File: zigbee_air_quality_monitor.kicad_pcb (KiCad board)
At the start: 4 copper layers, 19.8 x 50.9 mm, 37 parts, among them J1 USB_C_Receptacle_USB2.0, J2 QWIIC, J3 Conn_02x02_Odd_Even, SW1 PAIR_BTN, SW2 USER_BTN, U1 USBLC6-2SC6, U2 BT840, U3 XC6206P332MR, U4 SCD41-D-R2, U6 TXS0102DCU

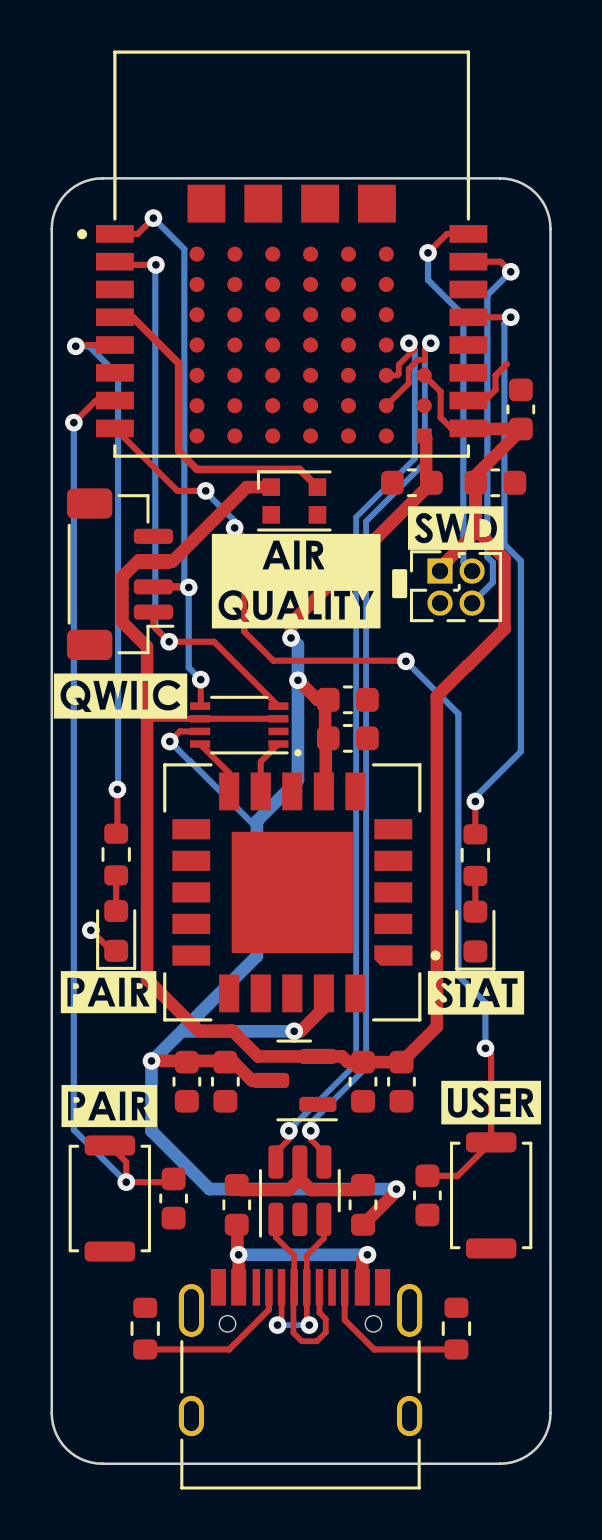
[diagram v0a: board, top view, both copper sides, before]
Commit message: Added inner GND planes, backside silkscreen label
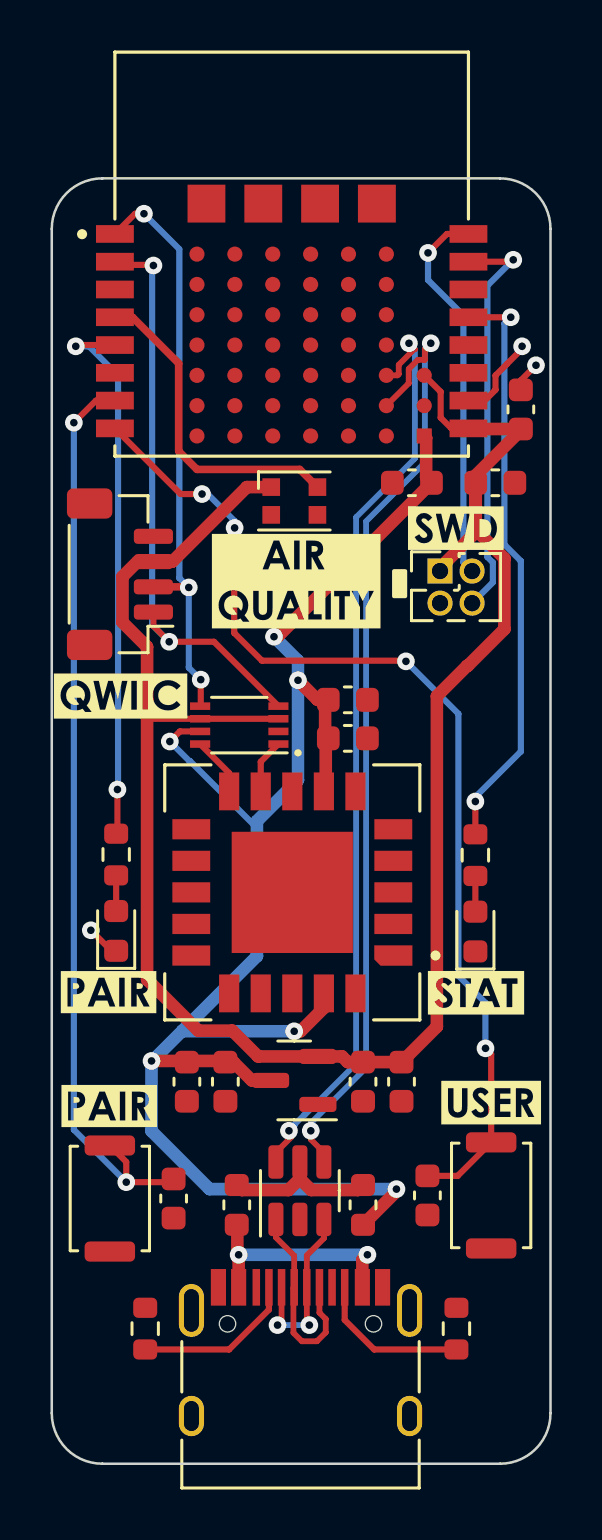
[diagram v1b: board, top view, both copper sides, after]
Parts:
- added G***: LOGO, LOGO, B.Cu at (131.7, 95.8)
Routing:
- net GND: track 3.80 -> 5.97 mm, vias 1 -> 3
- net VCC: track 68.5 -> 69.1 mm
- added copper zone on In1.Cu, net GND
- added copper zone on In2.Cu, net GND
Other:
- board text added: "Jan Gnip rev1 03/24"

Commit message: Routing done, via stitching done
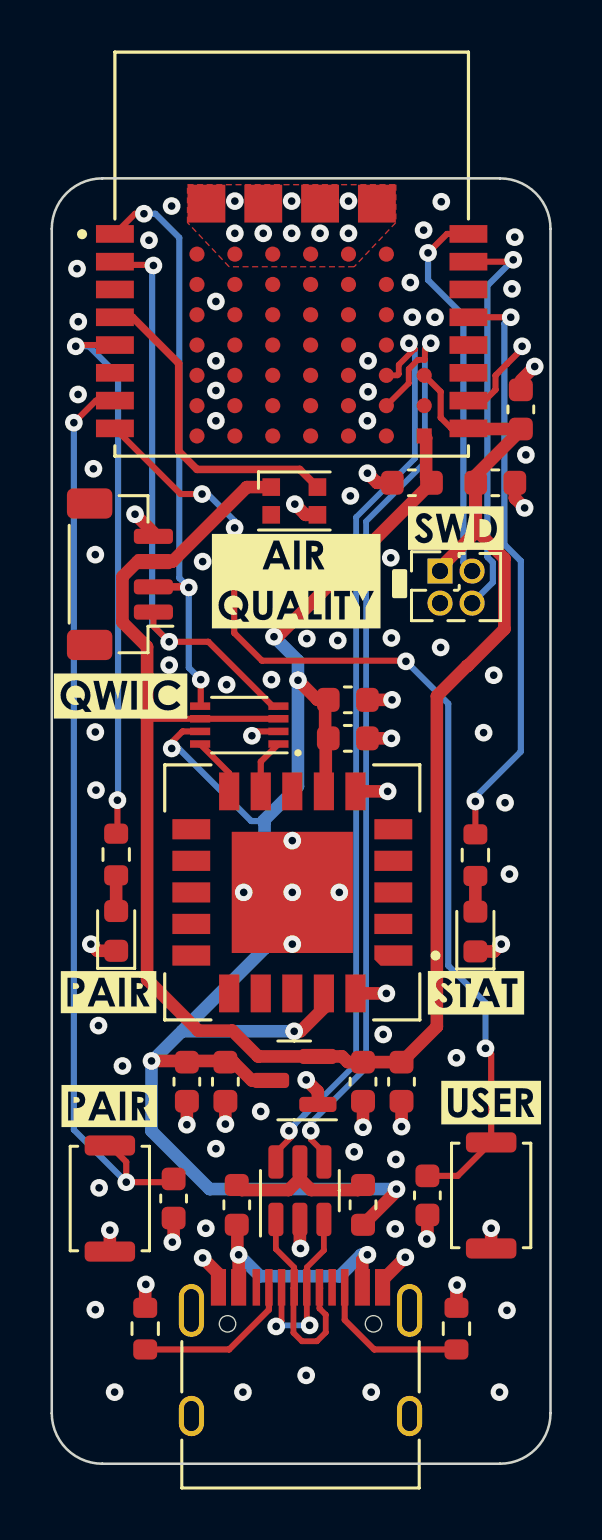
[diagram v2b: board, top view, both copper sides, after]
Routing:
- net GND: track 5.97 -> 31.5 mm, vias 3 -> 96
- net /USB_FUSE: track 8.98 -> 9.69 mm
- added copper zone on F.Cu, net GND

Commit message: Fixed silkscreen logo designator to make KiBot happy
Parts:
- renumbered G*** to G1
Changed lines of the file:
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@@
     (at 131.7 95.85 180)
     (attr board_only exclude_from_pos_files exclude_from_bom)
-    (fp_text reference "G***" (at 0 0) (layer "B.SilkS") hide
+    (fp_text reference "G1" (at 0 0) (layer "B.SilkS") hide
         (effects (font (size 1.524 1.524) (thickness 0.3)) (justify mirror))
     )

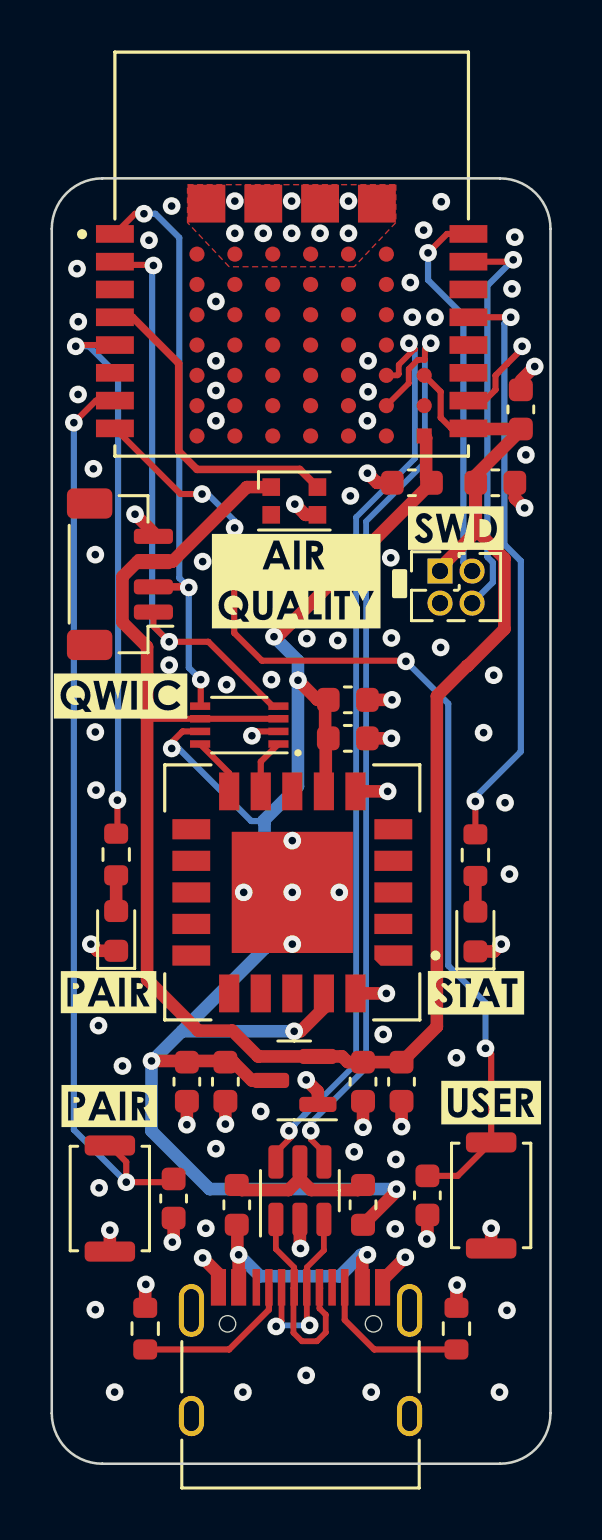
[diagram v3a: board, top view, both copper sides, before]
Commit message: Fixed QWIIC connector footprint and model
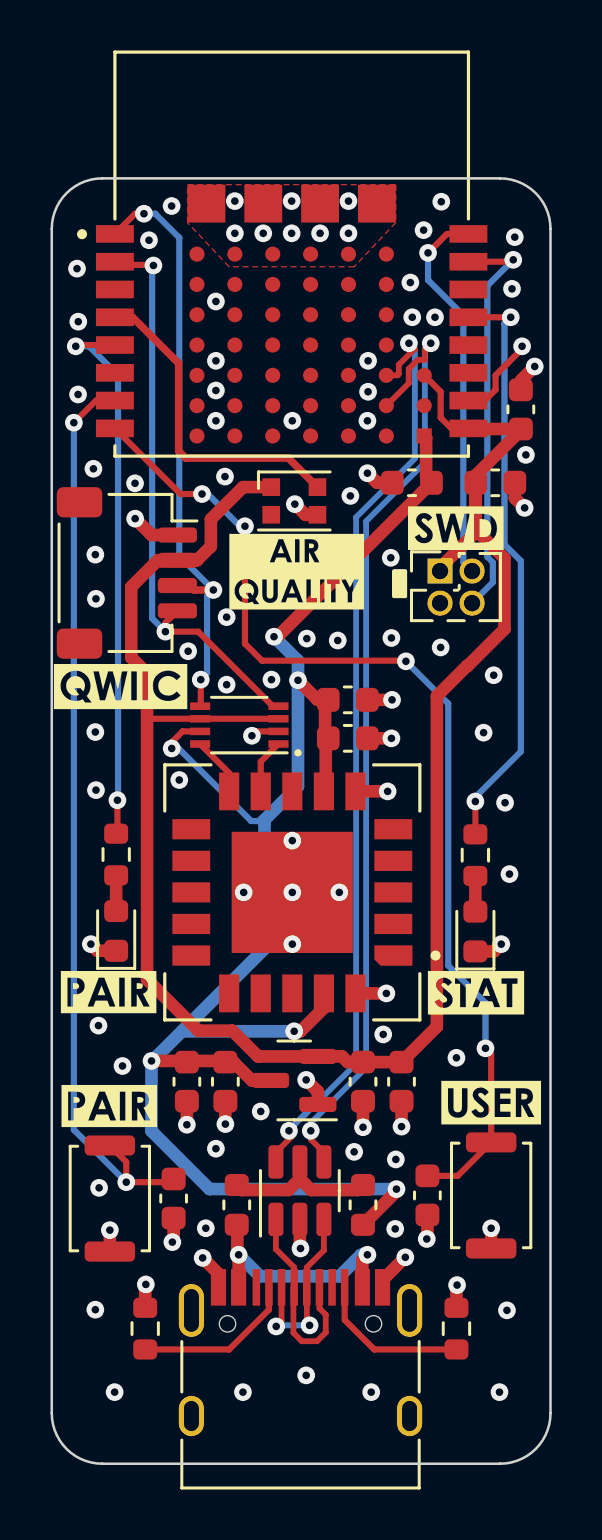
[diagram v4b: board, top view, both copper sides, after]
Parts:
- J2: footprint Connector_JST:JST_SH_BM04B-SRSS-TB_1x04-1MP_P1.00mm_Vertical -> Connector_JST:JST_SH_SM04B-SRSS-TB_1x04-1MP_P1.00mm_Horizontal
- kibuzzard-63D64589: footprint kibuzzard-63D64589 -> footprint
- moved kibuzzard-63D64589 0.38 mm to (131.8, 104.8)
- moved kibuzzard-63D6450F 0.38 mm to (124.8, 109.3)
- moved J2 0.28 mm to (125.1, 104.8), turned to -90 degrees
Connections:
- J1 pad S1: unconnected-(J1-SHIELD-PadS1) -> (no net)
- J2 pad 1: /I2C_SCL_3V3 -> GND
- J2 pad 2: /I2C_SDA_3V3 -> +3.3V
- J2 pad 3: +3.3V -> /I2C_SDA_3V3
- J2 pad 4: GND -> /I2C_SCL_3V3
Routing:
- net GND: track 31.5 -> 32.3 mm, vias 96 -> 101
- net /I2C_SCL_3V3: track 23.6 -> 23.0 mm

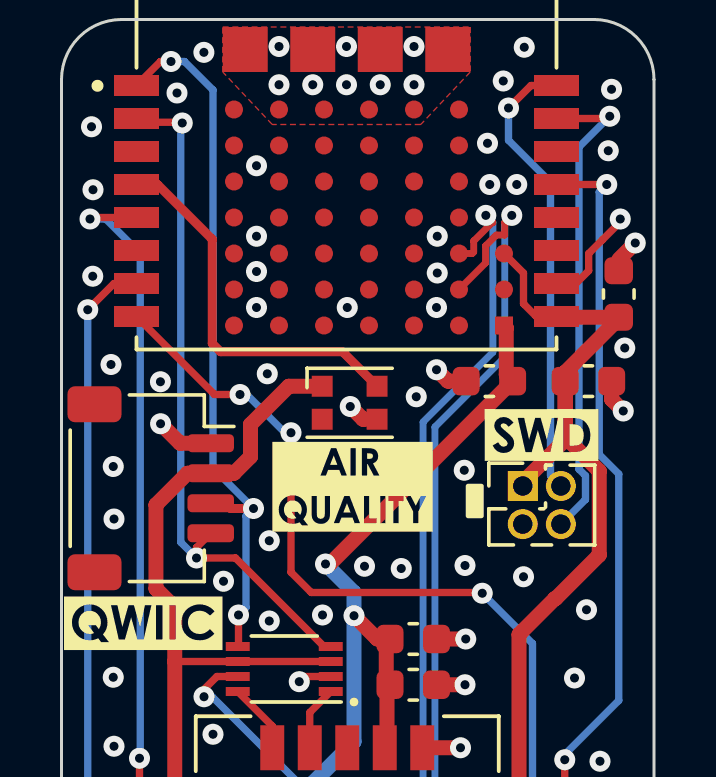
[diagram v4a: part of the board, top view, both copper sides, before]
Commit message: Changed supply voltage for WS2812-2020 LED to 5V
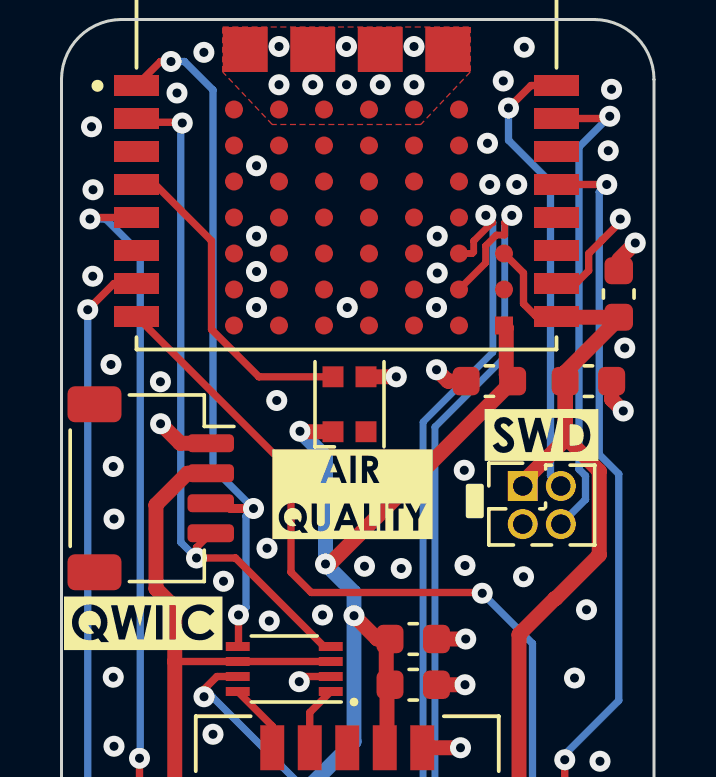
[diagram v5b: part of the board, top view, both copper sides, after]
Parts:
- moved kibuzzard-63D64589 0.25 mm to (131.8, 105.0)
- moved D3 0.05 mm to (131.7, 102.0), turned to 90 degrees
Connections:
- D3 pad 1: +3.3V -> VCC
- J1 pad S1: (no net) -> unconnected-(J1-SHIELD-PadS1)
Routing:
- net VCC: track 69.1 -> 75.0 mm, vias 6 -> 7
- net +3.3V: track 77.6 -> 72.1 mm
- net /AIR_QUALITY_LED: track 12.8 -> 10.9 mm
- net /USER_BTN: track 41.6 -> 40.8 mm, vias 4 -> 2
- net GND: track 32.3 -> 32.2 mm, vias 101 -> 100

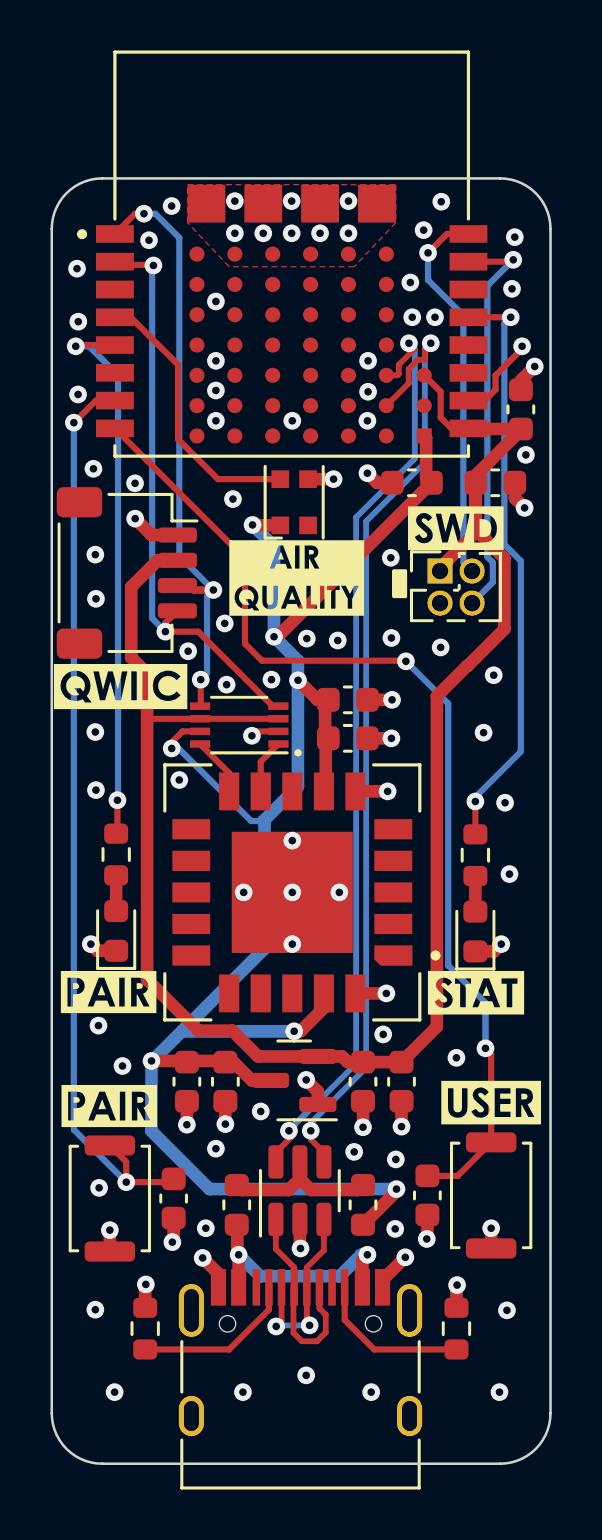
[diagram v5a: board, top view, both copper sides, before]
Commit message: Fixed clipped silkscreen, ERC+DRC warnings
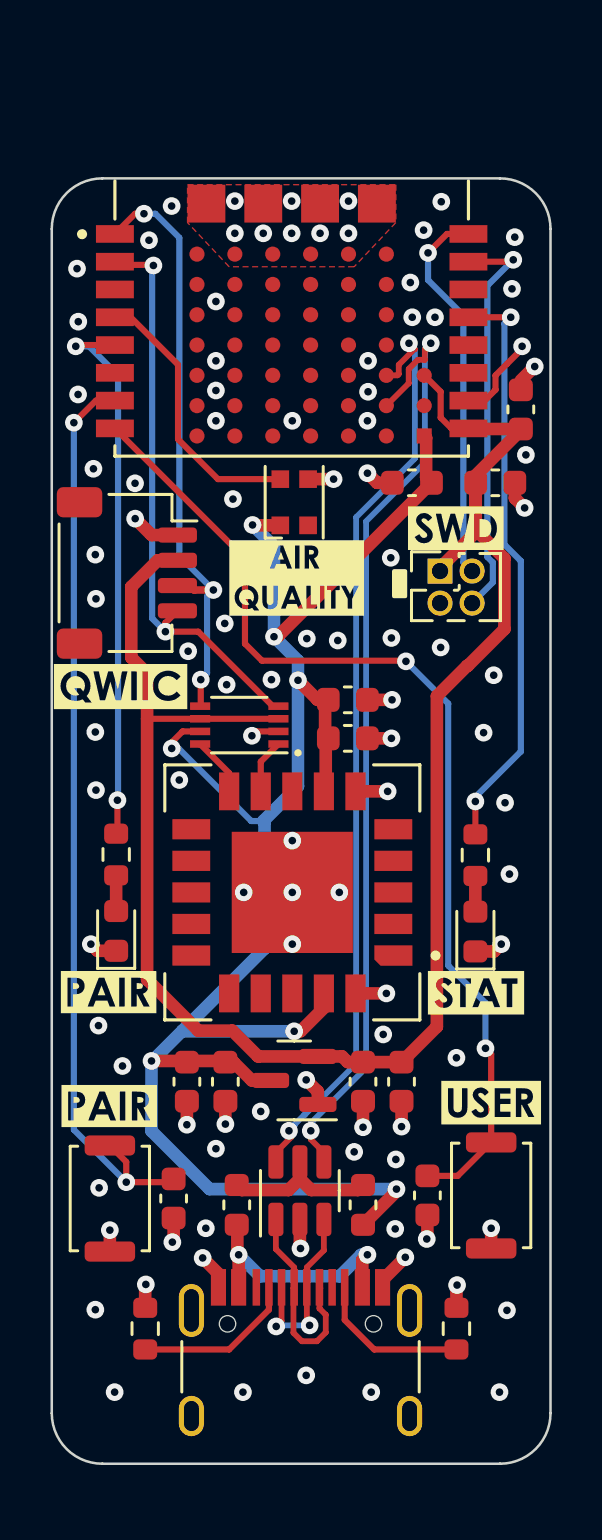
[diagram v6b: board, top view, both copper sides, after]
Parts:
- D3: value WS2812B -> WS2812B-2020
- U4: value SCD41-D-R2 -> SCD40-D-R2
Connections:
- J1 pad S1: unconnected-(J1-SHIELD-PadS1) -> (no net)
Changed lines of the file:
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@@
   (net 82 "/PAIR_BTN")
   (net 83 "/USER_BTN")
-  (net 84 "unconnected-(J1-SHIELD-PadS1)")
   (footprint "Resistor_SMD:R_0603_1608Metric" (layer "F.Cu")
     (at 138.125 134.75 -90)
@@
         (effects (font (size 1 1) (thickness 0.15)))
     )
-    (fp_text value "SCD41-D-R2" (at 4.225 6.935) (layer "F.Fab")
+    (fp_text value "SCD40-D-R2" (at 4.225 6.935) (layer "F.Fab")
         (effects (font (size 1 1) (thickness 0.15)))
     )
@@
     (fp_line (start -4.7 -1.9) (end -4.7 0.1)
       (stroke (width 0.12) (type solid)) (layer "F.SilkS"))
-    (fp_line (start -4.7 2) (end -4.7 3.9)
-      (stroke (width 0.12) (type solid)) (layer "F.SilkS"))
-    (fp_line (start -4.7 3.9) (end 4.7 3.9)
-      (stroke (width 0.12) (type solid)) (layer "F.SilkS"))
     (fp_line (start 4.7 -1.9) (end 4.7 0.1)
       (stroke (width 0.12) (type solid)) (layer "F.SilkS"))
-    (fp_line (start 4.7 2) (end 4.7 3.9)
-      (stroke (width 0.12) (type solid)) (layer "F.SilkS"))
     (fp_line (start -5.32 -5.27) (end -5.32 4.15)
       (stroke (width 0.05) (type solid)) (layer "F.CrtYd"))
@@
     (fp_line (start 5.32 -5.27) (end 5.32 4.15)
       (stroke (width 0.05) (type solid)) (layer "F.CrtYd"))
-    (fp_line (start -4.47 -3.65) (end -4.47 3.65)
+    (fp_line (start -4.47 -3.65) (end -4.47 2.2)
       (stroke (width 0.1) (type solid)) (layer "F.Fab"))
     (fp_line (start -4.47 -3.65) (end 4.47 -3.65)
       (stroke (width 0.1) (type solid)) (layer "F.Fab"))
-    (fp_line (start -4.47 3.65) (end 4.47 3.65)
-      (stroke (width 0.1) (type solid)) (layer "F.Fab"))
-    (fp_line (start 4.47 -3.65) (end 4.47 3.65)
+    (fp_line (start 4.47 -5.1) (end 4.47 2.2)
       (stroke (width 0.1) (type solid)) (layer "F.Fab"))
     (pad "" np_thru_hole circle (at -2.89 -2.6) (size 0.65 0.65) (drill 0.65) (layers "*.Cu" "*.Mask"))
@@
       (net 1 "GND") (pinfunction "GND") (pintype "passive"))
     (pad "S1" thru_hole oval (at -4.32 -3.13) (size 1 2.1) (drill oval 0.6 1.7) (layers "*.Cu" "*.Mask")
-      (net 84 "unconnected-(J1-SHIELD-PadS1)") (pinfunction "SHIELD") (pintype "passive+no_connect"))
+      (pinfunction "SHIELD") (pintype "passive+no_connect"))
     (pad "S1" thru_hole oval (at -4.32 1.05) (size 1 1.6) (drill oval 0.6 1.2) (layers "*.Cu" "*.Mask")
-      (net 84 "unconnected-(J1-SHIELD-PadS1)") (pinfunction "SHIELD") (pintype "passive+no_connect"))
+      (pinfunction "SHIELD") (pintype "passive+no_connect"))
     (pad "S1" thru_hole oval (at 4.32 -3.13) (size 1 2.1) (drill oval 0.6 1.7) (layers "*.Cu" "*.Mask")
-      (net 84 "unconnected-(J1-SHIELD-PadS1)") (pinfunction "SHIELD") (pintype "passive+no_connect"))
+      (pinfunction "SHIELD") (pintype "passive+no_connect"))
     (pad "S1" thru_hole oval (at 4.32 1.05) (size 1 1.6) (drill oval 0.6 1.2) (layers "*.Cu" "*.Mask")
-      (net 84 "unconnected-(J1-SHIELD-PadS1)") (pinfunction "SHIELD") (pintype "passive+no_connect"))
+      (pinfunction "SHIELD") (pintype "passive+no_connect"))
     (model "${KIPRJMOD}/libs/USBC_CONNECTOR/TYPE-C-31-M-12--3DModel-STEP-56544.STEP"
       (offset (xyz 0 -1.1 0))
@@
         (effects (font (size 1 1) (thickness 0.15)))
     )
-    (fp_text value "WS2812B" (at 0 2.2 90) (layer "F.Fab")
+    (fp_text value "WS2812B-2020" (at 0 2.2 90) (layer "F.Fab")
         (effects (font (size 1 1) (thickness 0.15)))
     )
@@
         (effects (font (size 1 1) (thickness 0.15)))
     )
-    (fp_line (start -7 -8) (end -7 -1.39)
-      (stroke (width 0.127) (type solid)) (layer "F.SilkS"))
-    (fp_line (start -7 -8) (end 7 -8)
+    (fp_line (start -7 -2.9) (end -7 -1.39)
       (stroke (width 0.127) (type solid)) (layer "F.SilkS"))
     (fp_line (start -7 7.59) (end -7 8)
@@
     (fp_line (start -7 8) (end 7 8)
       (stroke (width 0.127) (type solid)) (layer "F.SilkS"))
-    (fp_line (start 7 -8) (end 7 -1.39)
+    (fp_line (start 7 -2.9) (end 7 -1.39)
       (stroke (width 0.127) (type solid)) (layer "F.SilkS"))
     (fp_line (start 7 8) (end 7 7.59)

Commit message: Fixed SCD footprint name
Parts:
- U4: footprint zigbee_air_quality_monitor:XDCR_SCD41-D-R2 -> zigbee_air_quality_monitor:XDCR_SCD40-D-R2
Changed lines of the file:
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@@
     )
   )
-  (footprint "zigbee_air_quality_monitor:XDCR_SCD41-D-R2" (layer "F.Cu")
+  (footprint "zigbee_air_quality_monitor:XDCR_SCD40-D-R2" (layer "F.Cu")
     (at 131.625 117.475 180)
     (property "MANUFACTURER" "Sensirion")
